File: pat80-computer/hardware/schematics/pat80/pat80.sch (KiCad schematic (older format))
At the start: 3 parts, among them U1 Z80CPU, U2 256k (32k x 8) SRAM, U3 256k (32k x 8) EEPROM

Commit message: Removed symbol using third party library
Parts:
- removed U2: 256k (32k x 8) SRAM, DIP28, symbol idleengineer:HM62256BLP-7
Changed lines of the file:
@@
-$EndComp
-$Comp
-L idleengineer:HM62256BLP-7 U2
-U 1 1 604FA19C
-P 6700 3350
-F 0 "U2" V 6746 2506 50  0000 R CNN
-F 1 "256k (32k x 8) SRAM" V 6655 2506 50  0000 R CNN
-F 2 "DIP28" H 6700 3350 50  0001 C CIN
-F 3 "" H 6700 3350 50  0001 C CNN
-	1    6700 3350
-	0    -1   -1   0
 $EndComp
 $Comp

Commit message: Reset circuit
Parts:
- added C?: 10uF, symbol Device:C
- added C?: 100nF, symbol Device:C
- added C?: 56pF, symbol Device:C
- added R?: 270k, symbol Device:R
- added SW1: SW_Push, symbol Switch:SW_Push
- added U4: 256k (32k x 8) SRAM, symbol Memory_EEPROM:28C256
- added U?: 74LS32, symbol 74xx:74LS32
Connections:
- net labels added: GND, VCC
- wire segments 70 -> 92
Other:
- note added: "0.1 alpha"
- note added: "Reset circuit with debouncing\nand power-on-reset"
- note added: "Smoothing caps"
- moved on the sheet: U1, U3

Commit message: WIP Schematics
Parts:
- added C? (x2): 30pF, symbol Device:C
- added C? (x2): 100nF, symbol Device:C
- added C? (x2): 56pF, symbol Device:C
- added C?: 10uF, symbol Device:C
- added D?: LED, symbol Device:LED
- added J?: panel_btn_rst, symbol Connector:Conn_01x01_Male
- added J?: panel_btn_brk, symbol Connector:Conn_01x01_Male
- added J?: panel_led_halt, symbol Connector:Conn_01x01_Male
- added R?: 3,3M, symbol Device:R
- added R? (x2): 10k, symbol Device:R
- added R?: 470, symbol Device:R
- added SW?: Break, symbol Switch:SW_Push
- added U11: 74HC04, symbol 74xx:74HC04
- added Y?: 4Mhz, symbol Device:Crystal
- gave numbers to parts that had none: 1
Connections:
- net GND: now also C?.1, C?.1, C?.1, C?.1, C?.2, C?.2, C?.2, SW?.1
- net VCC: now also C?.2, C?.2, C?.2, C?.2, R?.2, R?.2, R?.2
- net at U1.16 (~INT~): now also C?.1, J?.1 (Pin_1), R?.1, SW?.2
- net at U1.17 (~NMI~): now also R?.1
- net at U1.18 (~HALT~): now also D?.1 (K), J?.1 (Pin_1)
- net at U1.6 (~CLK~): now also U11.4
- net at C?.1, R?.2, SW1.2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: now also J?.1 (Pin_1)
- new net: C?.1, R?.1, U11.1, Y?.1
- new net: C?.1, R?.2, U11.2, U11.3, Y?.2
- new net: D?.2 (A), R?.1
- no-connect marks 0 -> 4
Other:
- note added: ""Break" button"
- note added: "Reset circuit with\ndebouncing and\npower-on-reset"
- note added: "System clock\n 4Mhz"
- note removed: "Reset circuit with debouncing\nand power-on-reset"
- moved on the sheet: C?, R?, SW1, U1, U10A, U3, U4

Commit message: Memory decoding, WIP IO decoding
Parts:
- added C?: 100nF, symbol Device:C
- added C?: 56pF, symbol Device:C
- added unit 2 of U10
- added unit 1 of U10
- added unit 1 of U11
- added unit 2 of U11
- added U?: 74LS138, symbol 74xx:74LS138
- U11: value 74HC04 -> 74LS32
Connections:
- net labels added: IOBUS, IOEN0, IOEN1, IOEN2, IOEN3, IOEN4, IOEN5, IOEN6, IOEN7, IORQ, RAMEN, RD, ROMEN, WR
- wire segments 137 -> 197
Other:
- note added: "I/O Decoding logic"
- note added: "Memory"
- note added: "Memory decoding logic"
- moved on the sheet: C?, D?, J?, R?, SW1, SW?, U1, U3, U4, Y?

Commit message: Almost finished transcribing mainboard schematics
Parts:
- added C14, C16: 100nF, symbol Device:C
- added C15, C17: 56pF, symbol Device:C
- added C20, C7: 470uF, symbol Device:C
- added C4: 0,22uF, symbol Device:C
- added C5: 0,1uF, symbol Device:C
- added J2: Power input, symbol Connector:Conn_01x02_Male
- added U21: 74HC244, symbol 74xx:74HC244
- added U22: 74HC245, symbol 74xx:74HC245
- added U30: LM7805_TO220, Package_TO_SOT_THT:TO-220-3_Vertical, symbol Regulator_Linear:LM7805_TO220
- gave numbers to parts that had none: 24
- renumbered U3 to U2, U4 to U3
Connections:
- net labels added: IOADDR0, IOADDR1, IOADDR2, IOADDR3, IOADDR4, IOD0, IOD1, IOD2, IOD3, IOD4, IOD5, IOD6, IOD7, IOGND, IOVCC, IOWR
- wire segments 197 -> 269
- no-connect marks 4 -> 15
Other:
- note added: "I/O Data transceiver"
- note added: "Power input"
- moved on the sheet: C1, C10, C11, C12, C13, C2, C3, C6, C8, C9, D1, J1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

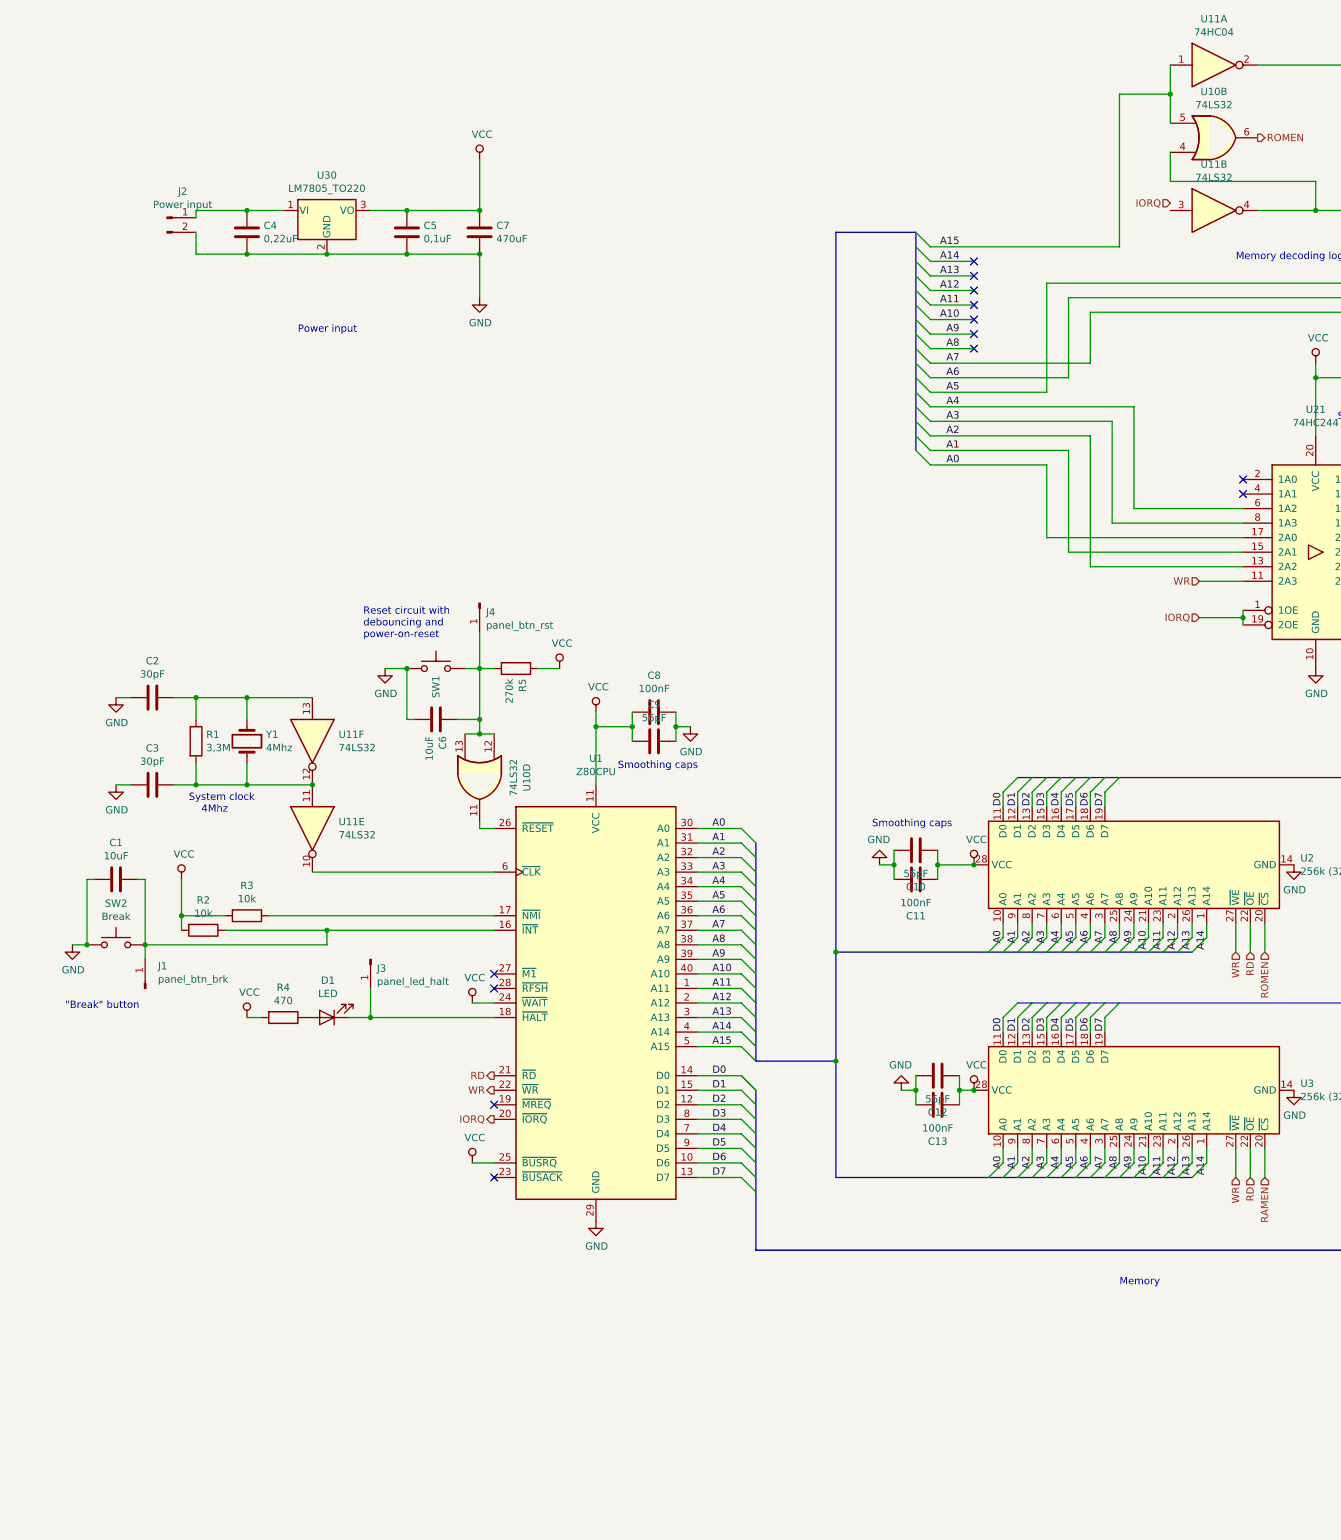
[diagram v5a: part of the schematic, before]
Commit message: Schematic complete, commit before assigning footprints
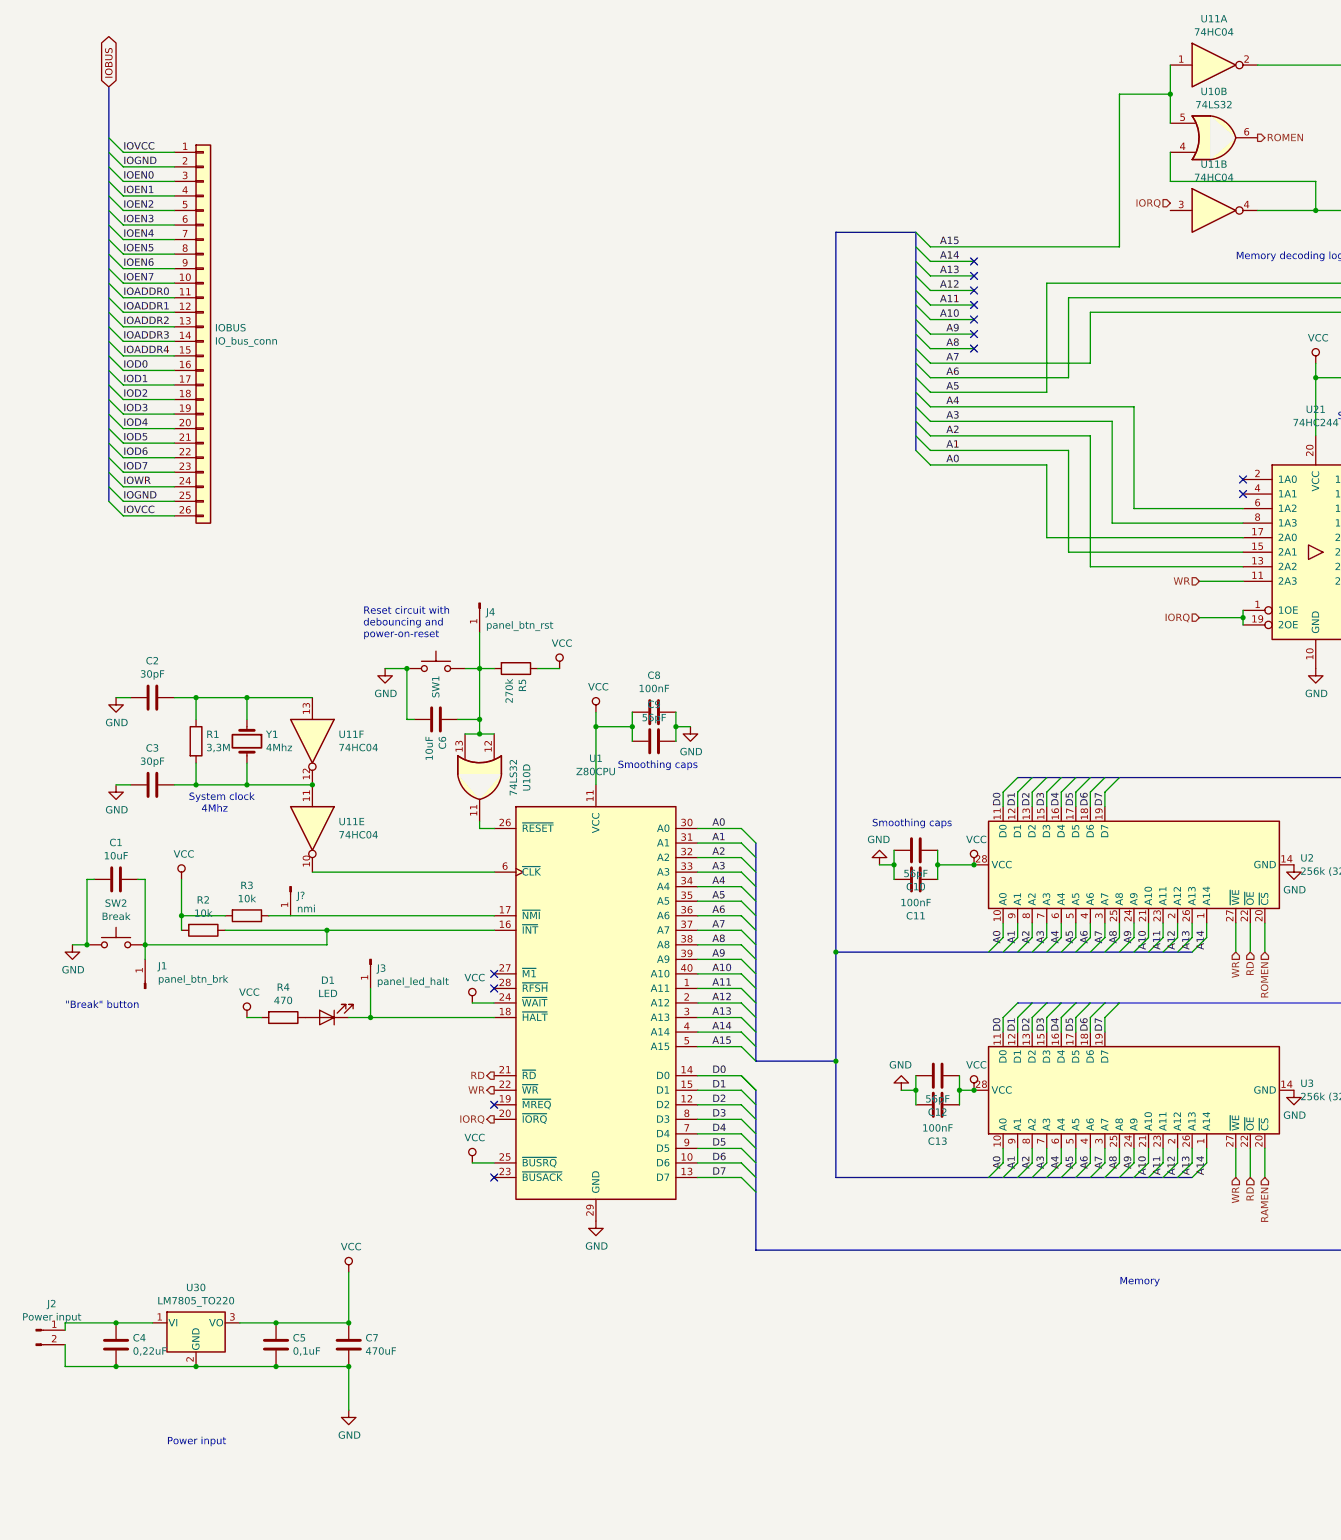
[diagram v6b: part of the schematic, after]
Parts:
- added IOBUS: IO_bus_conn, symbol Connector_Generic:Conn_01x26
- added J?: nmi, symbol Connector:Conn_01x01_Male
- U11: value 74LS32 -> 74HC04
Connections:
- net GND: now also IOBUS.2 (Pin_2), IOBUS.25 (Pin_25)
- net IOADDR0: now also IOBUS.11 (Pin_11)
- net IOADDR1: now also IOBUS.12 (Pin_12)
- net IOADDR2: now also IOBUS.13 (Pin_13)
- net IOADDR3: now also IOBUS.14 (Pin_14)
- net IOADDR4: now also IOBUS.15 (Pin_15)
- net IOD0: now also IOBUS.16 (Pin_16)
- net IOD1: now also IOBUS.17 (Pin_17)
- net IOD2: now also IOBUS.18 (Pin_18)
- net IOD3: now also IOBUS.19 (Pin_19)
- net IOD4: now also IOBUS.20 (Pin_20)
- net IOD5: now also IOBUS.21 (Pin_21)
- net IOD6: now also IOBUS.22 (Pin_22)
- net IOD7: now also IOBUS.23 (Pin_23)
- net IOEN0: now also IOBUS.3 (Pin_3)
- net IOEN1: now also IOBUS.4 (Pin_4)
- net IOEN2: now also IOBUS.5 (Pin_5)
- net IOEN3: now also IOBUS.6 (Pin_6)
- net IOEN4: now also IOBUS.7 (Pin_7)
- net IOEN5: now also IOBUS.8 (Pin_8)
- net IOEN6: now also IOBUS.9 (Pin_9)
- net IOEN7: now also IOBUS.10 (Pin_10)
- net IOWR: now also IOBUS.24 (Pin_24)
- net VCC: now also IOBUS.1 (Pin_1), IOBUS.26 (Pin_26)
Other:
- moved on the sheet: C4, C5, C7, J2, U30

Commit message: Schematics: assigned footprints, created ratsnest
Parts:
- C1, C10, C11, C12, C13, C14, C15, C16, C17, C18, C19, C2, C3, C4, C5, C6, C8, C9: footprint (none) -> Capacitor_THT:CP_Radial_Tantal_D6.0mm_P5.00mm
- C20, C7: footprint (none) -> Capacitor_THT:CP_Radial_D6.3mm_P2.50mm
- D1: footprint (none) -> LED_THT:LED_D5.0mm
- IOBUS1: renamed from IOBUS; footprint (none) -> Connector_PinHeader_2.54mm:PinHeader_1x26_P2.54mm_Horizontal
- J1, J3, J4: footprint (none) -> Connector_PinHeader_2.54mm:PinHeader_1x01_P2.54mm_Vertical
- J2: footprint (none) -> Connector_PinHeader_2.54mm:PinHeader_1x02_P2.54mm_Vertical
- J5: renamed from J?; footprint (none) -> Connector_PinHeader_2.54mm:PinHeader_1x01_P2.54mm_Vertical
- R1, R2, R3, R4, R5: footprint (none) -> Resistor_THT:R_Axial_DIN0207_L6.3mm_D2.5mm_P7.62mm_Horizontal
- SW1, SW2: footprint (none) -> Button_Switch_THT:SW_Tactile_Straight_KSA0Axx1LFTR
- U1: footprint (none) -> Package_DIP:DIP-40_W15.24mm_Socket_LongPads
- U10: value 74LS32 -> 74HC32; footprint (none) -> Package_DIP:DIP-14_W7.62mm_Socket_LongPads
- U11: footprint (none) -> Package_DIP:DIP-14_W7.62mm_Socket_LongPads
- U2, U3: footprint (none) -> Package_DIP:DIP-28_W15.24mm_Socket_LongPads
- U20: value 74LS138 -> 74HC138; footprint (none) -> Package_DIP:DIP-16_W7.62mm_Socket_LongPads
- U21, U22: footprint (none) -> Package_DIP:DIP-20_W7.62mm_Socket_LongPads
- Y1: footprint (none) -> Crystal:Crystal_HC18-U_Vertical

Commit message: Connector description
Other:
- note added: "IOBUS connector is inserted into a passive backplane\nthat can be seen in the Backplane schematics."
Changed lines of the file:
@@
 Wire Bus Line
 	1550 1150 1550 4000
+Text Notes 950  4450 0    50   ~ 0
+IOBUS connector is inserted into a passive backplane\nthat can be seen in the Backplane schematics.
 $EndSCHEMATC
